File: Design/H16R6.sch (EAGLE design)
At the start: 111 parts, among them IC1 74LVC2T45HK3-7, P1 HEXABIT_17.32, U1 STM32G0B1CEU6N, X1 XTALL_CSTCE8M00G52

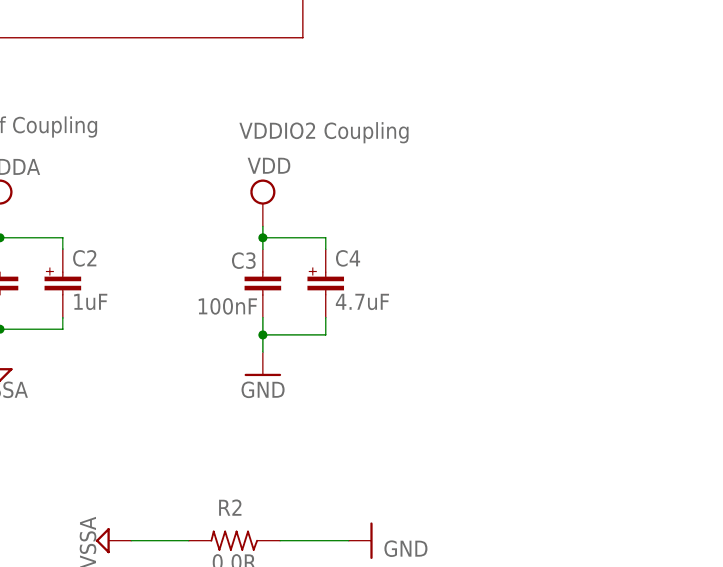
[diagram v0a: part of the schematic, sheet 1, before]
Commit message: Edit the logo Add the TVS diode
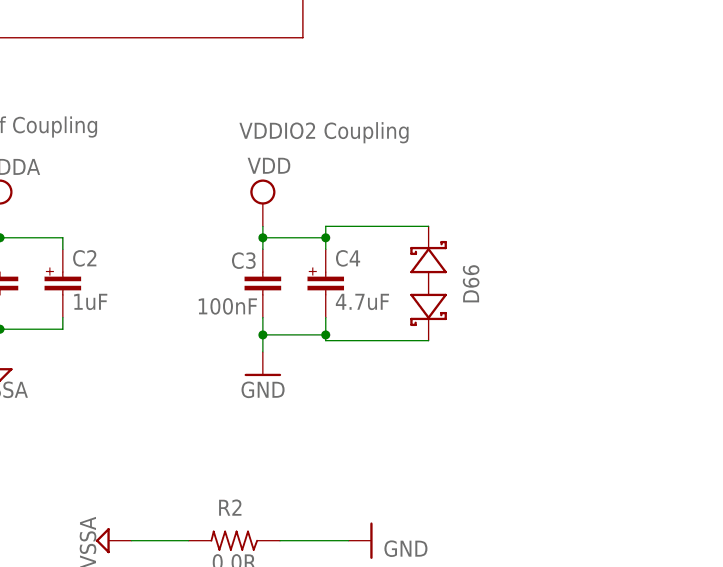
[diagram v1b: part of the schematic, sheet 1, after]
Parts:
- added D66: BOURNS_CDSOD323-T03SCBOURNS_CDSOD323-T03SC_0_0, HEXABITZ_RCLS:BOURNS_CDSOD323-T03SCBOURNS_CDSOD323-T03SC_0_0
- added TRIMBLE-LOGO1: HEXA-LOGO, HEXABITZ_USER_INTERFACE_PARTS:HEXA-LOGO
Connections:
- net GND: now also D66.A
- net VDD: now also D66.C

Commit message: no message
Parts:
- removed C1: 100nF, HEXABITZ_RCLS:C-0402
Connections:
- net +VS: no longer C1.1
- net CKI: now also SERIAL_IN.1; no longer SERIAL_OUT.1
- net CKO: now also SERIAL_OUT.1; no longer SERIAL_IN.1
- net GND: no longer C1.2
- net SDI: now also SERIAL_IN.2; no longer SERIAL_OUT.2
- net SDO: now also SERIAL_OUT.2; no longer SERIAL_IN.2
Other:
- moved on the sheet: C16, C20, C23, C24, C25, C26, C27, C9, SERIAL_IN, SERIAL_OUT

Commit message: Replace the led APA-102-2020-6 with APA-102-2020-8
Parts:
- added C1: 100nF, HEXABITZ_RCLS:C-0402
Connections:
- net +VS: now also C1.1
- net CKI: now also SERIAL_OUT.1; no longer SERIAL_IN.1
- net CKO: now also SERIAL_IN.1; no longer SERIAL_OUT.1
- net GND: now also C1.2
- net SDI: now also SERIAL_OUT.2; no longer SERIAL_IN.2
- net SDO: now also SERIAL_IN.2; no longer SERIAL_OUT.2
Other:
- moved on the sheet: C16, C20, C23, C24, C25, C26, C27, C9, SERIAL_IN, SERIAL_OUT

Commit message: Fix the clearance and soldermask issues Replace the 0603 4.7uF tant cap with ceramic cap in the BOM
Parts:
- removed C1: 100nF, HEXABITZ_RCLS:C-0402
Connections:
- net +VS: no longer C1.1
- net CKI: now also SERIAL_IN.1; no longer SERIAL_OUT.1
- net CKO: now also SERIAL_OUT.1; no longer SERIAL_IN.1
- net GND: no longer C1.2
- net SDI: now also SERIAL_IN.2; no longer SERIAL_OUT.2
- net SDO: now also SERIAL_OUT.2; no longer SERIAL_IN.2
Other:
- moved on the sheet: C16, C20, C23, C24, C25, C26, C27, C9, SERIAL_IN, SERIAL_OUT
